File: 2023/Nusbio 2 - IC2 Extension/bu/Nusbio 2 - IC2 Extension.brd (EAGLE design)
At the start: 90 x 90 mm, 18 parts

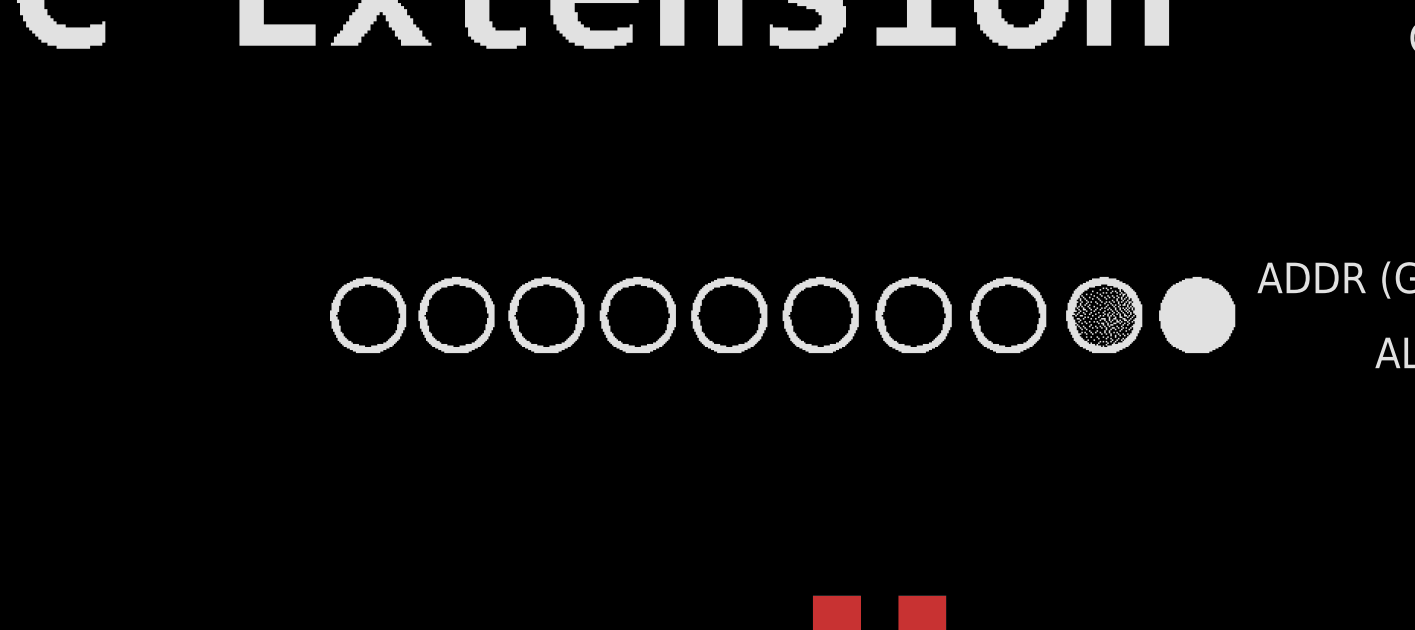
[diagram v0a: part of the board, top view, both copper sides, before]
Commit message: Nusbio v2 pcb and SPIExtension v 1 2023/05
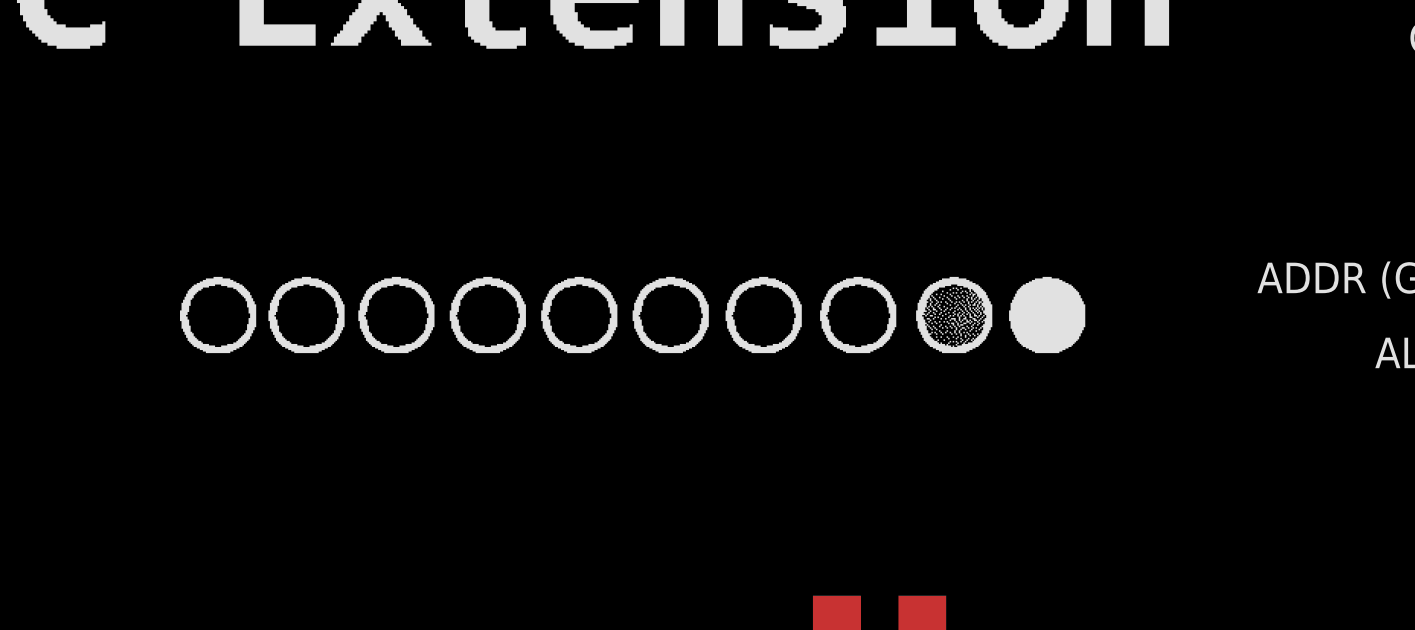
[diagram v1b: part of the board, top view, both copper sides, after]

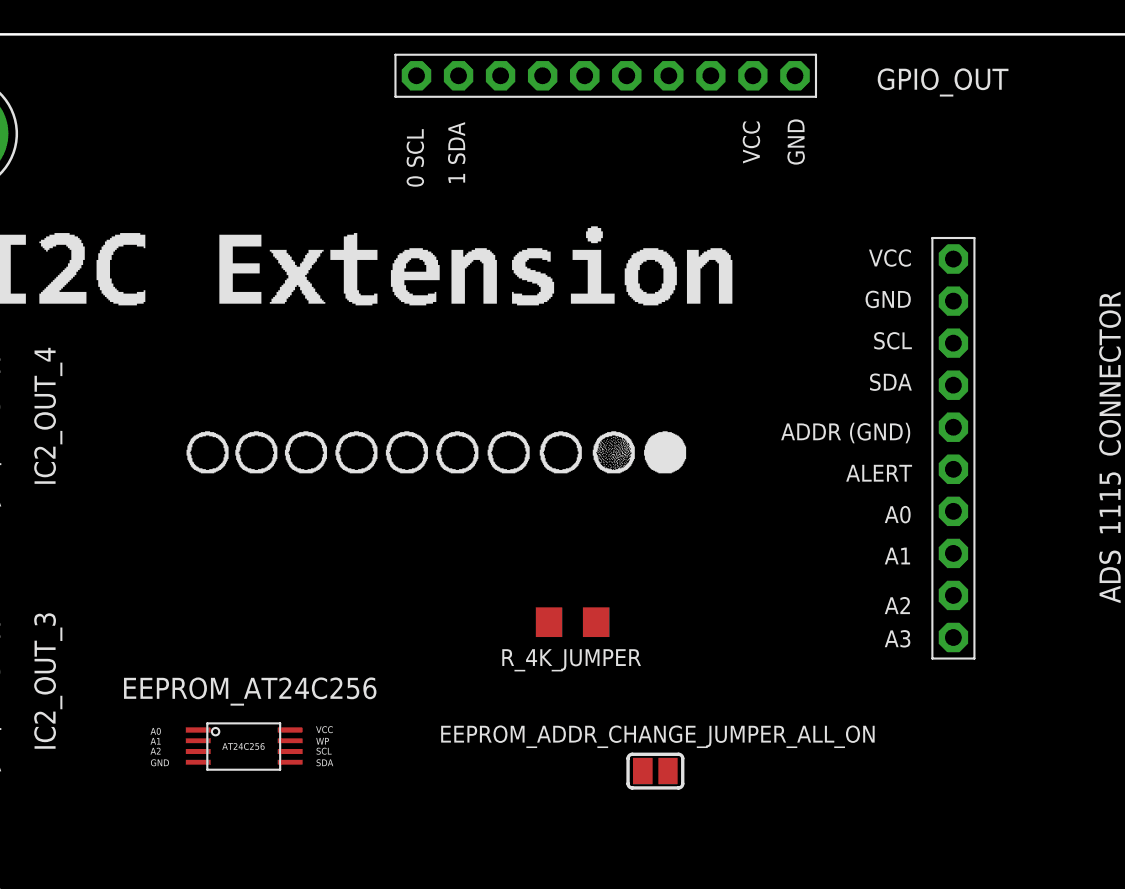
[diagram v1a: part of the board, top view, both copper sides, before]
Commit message: Fix Nusbio I2Cextension with right eeprom format
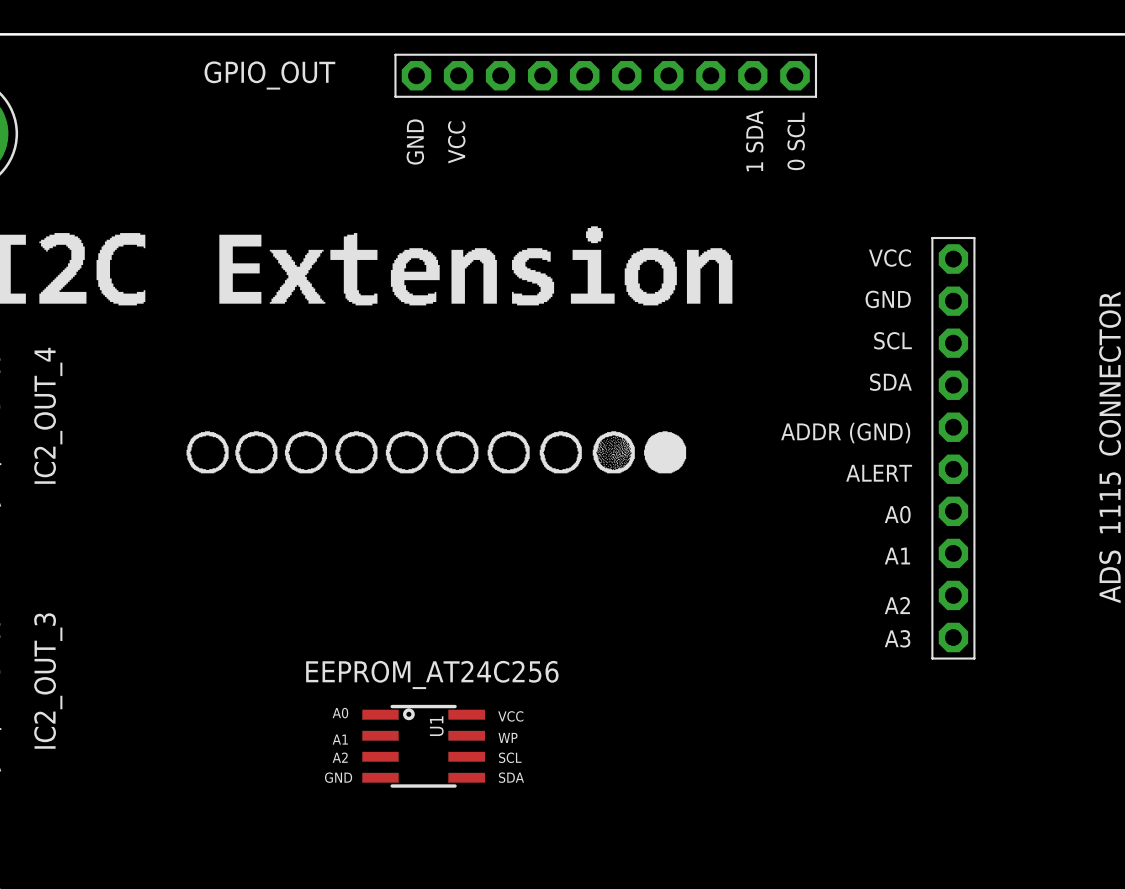
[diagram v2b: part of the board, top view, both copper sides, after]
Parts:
- removed EEPROM_ADDR_CHANGE_JUMPER_ALL_ON: (no value), microbuilder:SOLDERJUMPER_REFLOW
- removed EEPROM_AT24C256: DECADE-AT24C256-10TI-2.7, DECADE-libraries20151104:DECADE-AT24CXX
- removed R_4K_JUMPER: (no value), adafruit:R1206
- added U1: (no value), microbuilder:SOIC8_150MIL
- turned GPIO_OUT to 180 degrees
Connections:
- removed net N$1: EEPROM_AT24C256.VCC
- removed net N$6: EEPROM_ADDR_CHANGE_JUMPER_ALL_ON.2, R_4K_JUMPER.1
- net GND: now also U1.1, U1.2, U1.3, U1.4, U1.7; no longer EEPROM_ADDR_CHANGE_JUMPER_ALL_ON.1, EEPROM_AT24C256.A0, EEPROM_AT24C256.A1, EEPROM_AT24C256.A2, EEPROM_AT24C256.GND, EEPROM_AT24C256.WP
- net SCL: now also U1.6; no longer EEPROM_AT24C256.SCL
- net SDA: now also U1.5; no longer EEPROM_AT24C256.SDA
- net VCC: now also U1.8; no longer R_4K_JUMPER.2
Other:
- board text added: "PCBv2 - 2023.10"
- board text removed: "PCBv1 - 2023.05"
